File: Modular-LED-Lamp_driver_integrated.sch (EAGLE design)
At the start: 21 parts

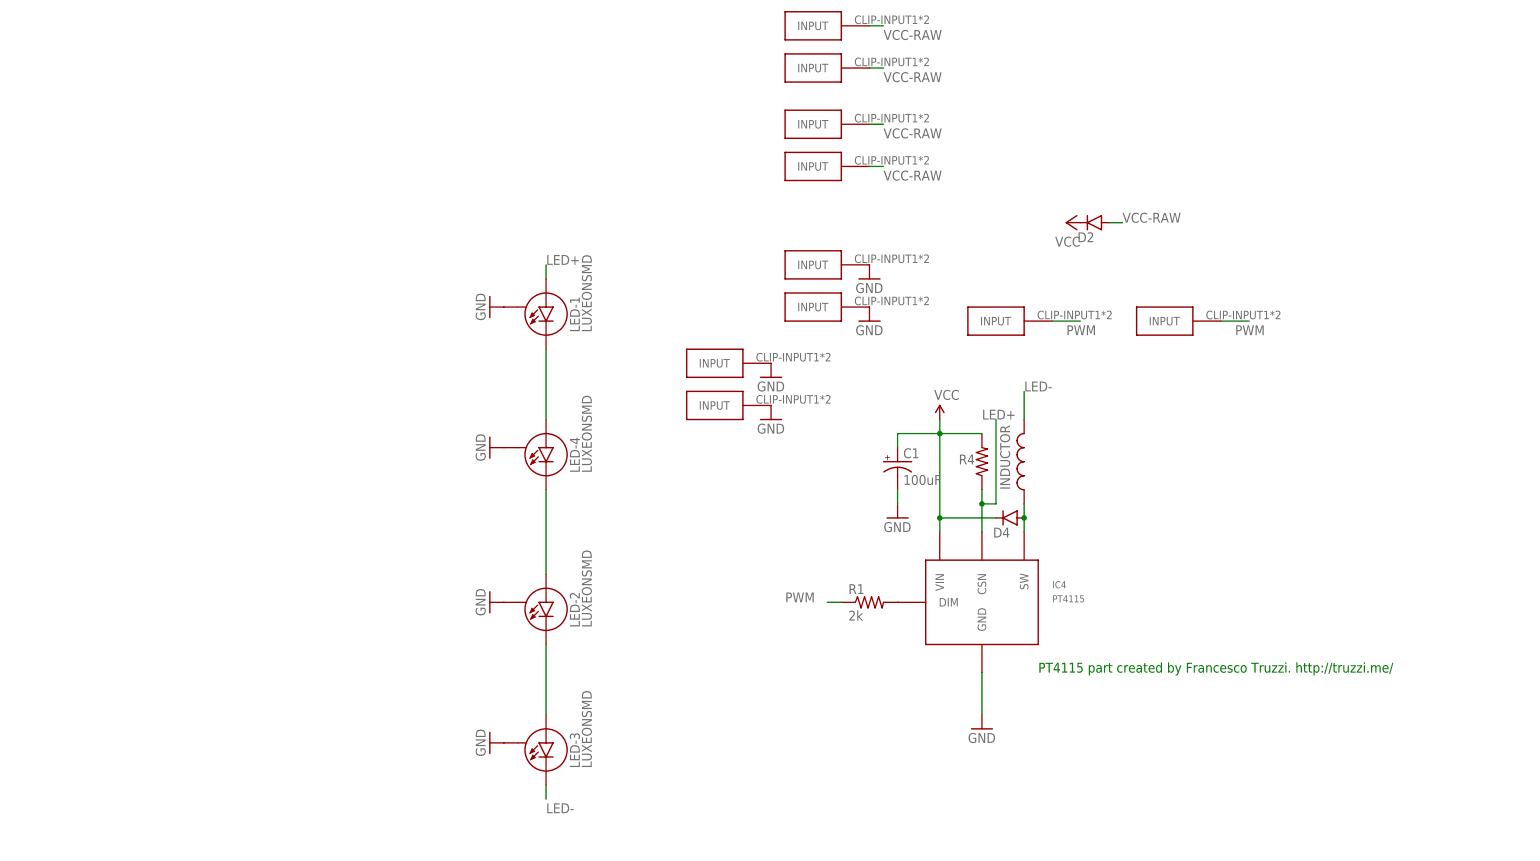
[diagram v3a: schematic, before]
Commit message: Added BOM, updated schematic and board for integrated variant
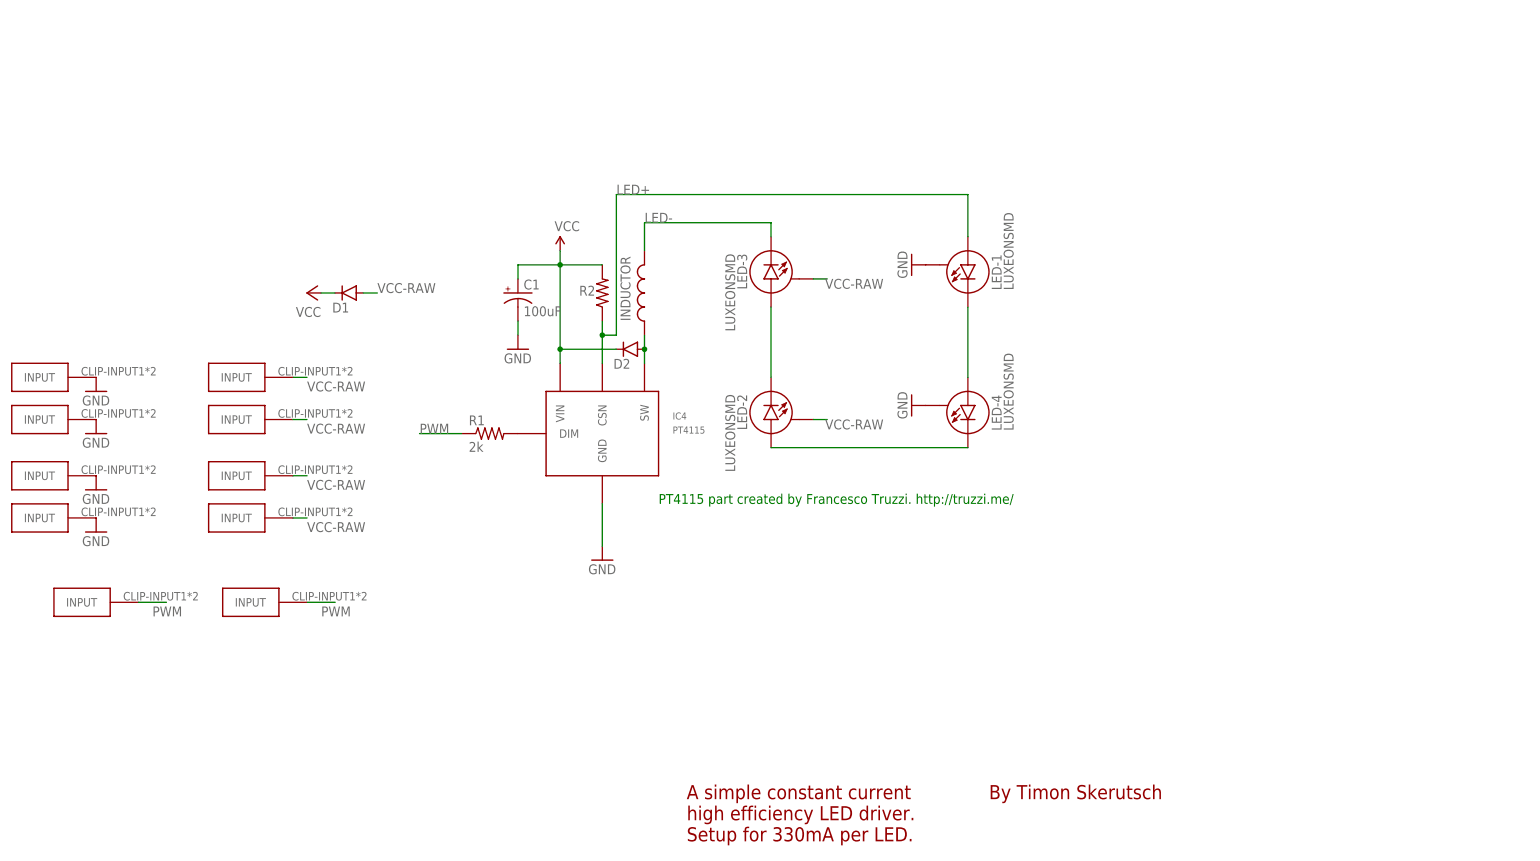
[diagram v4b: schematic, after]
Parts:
- removed D4: (no value), SparkFun-DiscreteSemi:DIODESMA-KIT
- removed R4: 0.3, SparkFun-Resistors:RESISTOR1206
- added D1: (no value), SparkFun-DiscreteSemi:DIODESMA-KIT
- added R2: 0.3, SparkFun-Resistors:RESISTOR1206
- GND-CLIP, GND-CLIP1, GND-CLIP2, GND-CLIP3: value GND -> FUSE-HOLDER-5X20MM
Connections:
- net GND: no longer LED-2.S, LED-3.S
- net LED+: now also R2.1; no longer R4.1
- net N$1: now also D2.A; no longer D4.A
- net VCC: now also D1.C, R2.2; no longer D4.C, R4.2
- net VCC-RAW: now also D1.A, LED-2.S, LED-3.S; no longer D2.A
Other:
- note added: "A simple constant current high efficiency LED driver. Setup for 330mA per LED."
- note added: "By Timon Skerutsch"
- moved on the sheet: C1, D2, IC4, INDUCTOR, LED-1, LED-2, LED-3, LED-4, R1
